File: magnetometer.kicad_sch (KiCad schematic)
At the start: 1 part, among them IC1 MMC5983MA

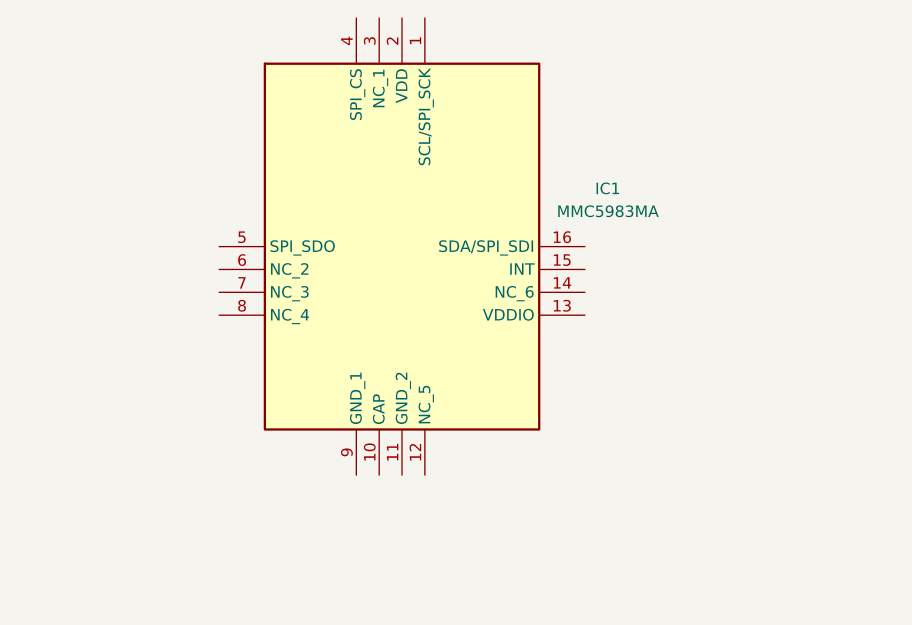
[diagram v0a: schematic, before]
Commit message: added circuitry for magnetometer, gyroscope and h-bridges
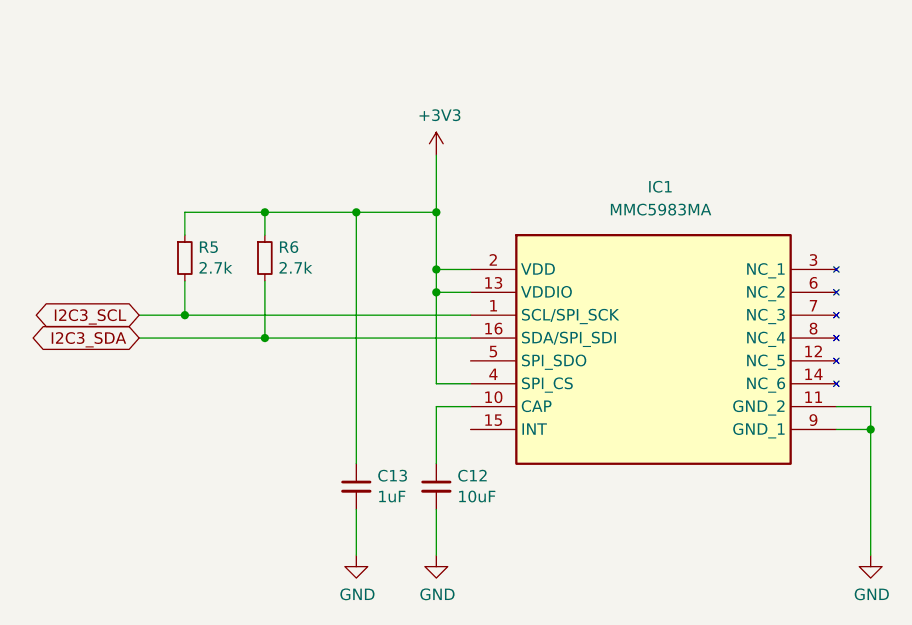
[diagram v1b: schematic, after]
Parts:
- added C12: 10uF, Capacitor_SMD:C_0805_2012Metric_Pad1.15x1.40mm_HandSolder, symbol Device:C_Small
- added C13: 1uF, Capacitor_SMD:C_0805_2012Metric_Pad1.15x1.40mm_HandSolder, symbol Device:C_Small
- added R5, R6: 2.7k, Resistor_SMD:R_0805_2012Metric_Pad1.15x1.40mm_HandSolder, symbol Device:R_Small
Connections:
- net I2C3_SCL: now reaches IC1.1 (SCL/SPI_SCK)
- net I2C3_SCL: now also R5.2
- net at IC1.10 (CAP): now also C12.1
- net GND: now reaches IC1.11 (GND_2)
- net GND: now also IC1.9 (GND_1), C12.2, C13.2
- net +3V3: now reaches IC1.13 (VDDIO)
- net +3V3: now also IC1.2 (VDD), IC1.4 (SPI_CS), C13.1, R5.1, R6.1
- net I2C3_SDA: now reaches IC1.16 (SDA/SPI_SDI)
- net I2C3_SDA: now also R6.2
